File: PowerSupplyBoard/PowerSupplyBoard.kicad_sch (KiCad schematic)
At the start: 96 parts, among them J101 BATTERY, J102 I2C, J103 USB_C, J104 PWR, J105 DATA1, Q101 BSH205G2A, Q102 DMP6050SSD, Q103 2N7002H, SW101 SW_SPDT, U101 TPS63070, U102 MCP73834T, U103 NCV33163, U104 CYPD3177-24LQ, U105 CS5173

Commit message: psu rev5 layout
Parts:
- removed R134: 33k, Resistor_SMD:R_0805_2012Metric, symbol Device:R_US
- added D108: SMPS, LED_THT:LED_D3.0mm, symbol Device:LED
- added R135: 470, Resistor_SMD:R_0805_2012Metric, symbol Device:R_US
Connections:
- net +3.3V: now also D108.2 (A)
- net GND: now also R135.2
- new net: D108.1 (K), R135.1
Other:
- note removed: "R134 helps us discharge the decoupling caps after power down"
- moved on the sheet: C101, C102, C103, C104, C105, C107, C108, C110, C111, C112, C113, C114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

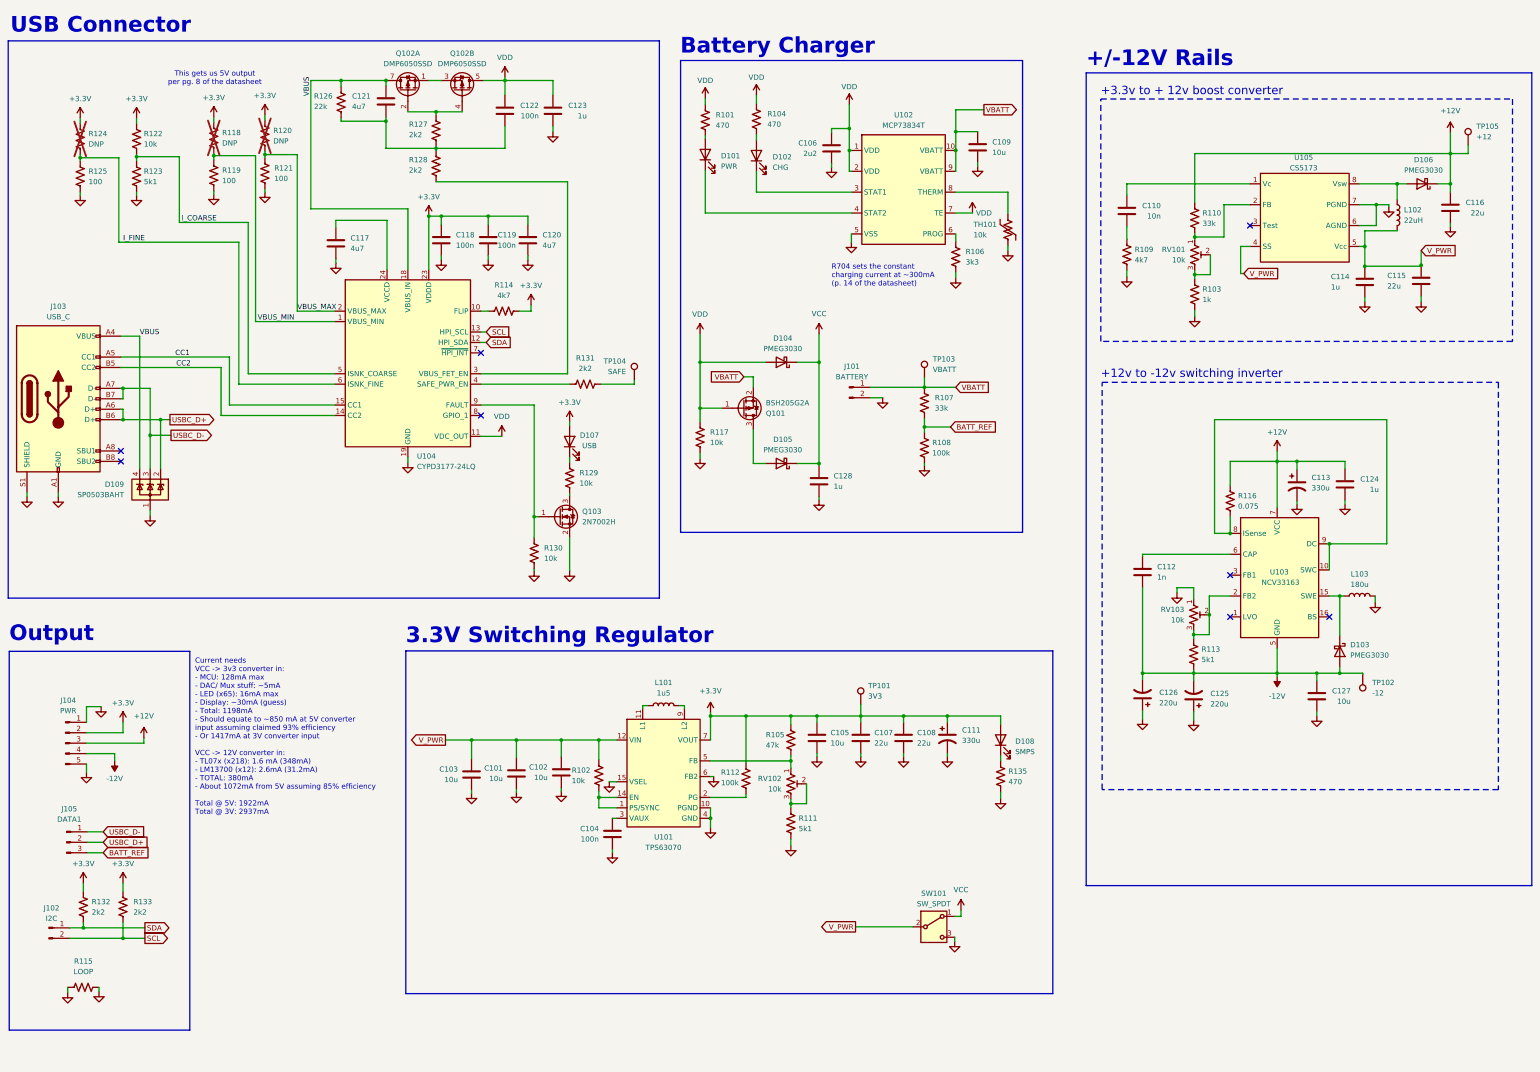
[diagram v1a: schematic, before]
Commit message: psu rev5 sent to fab
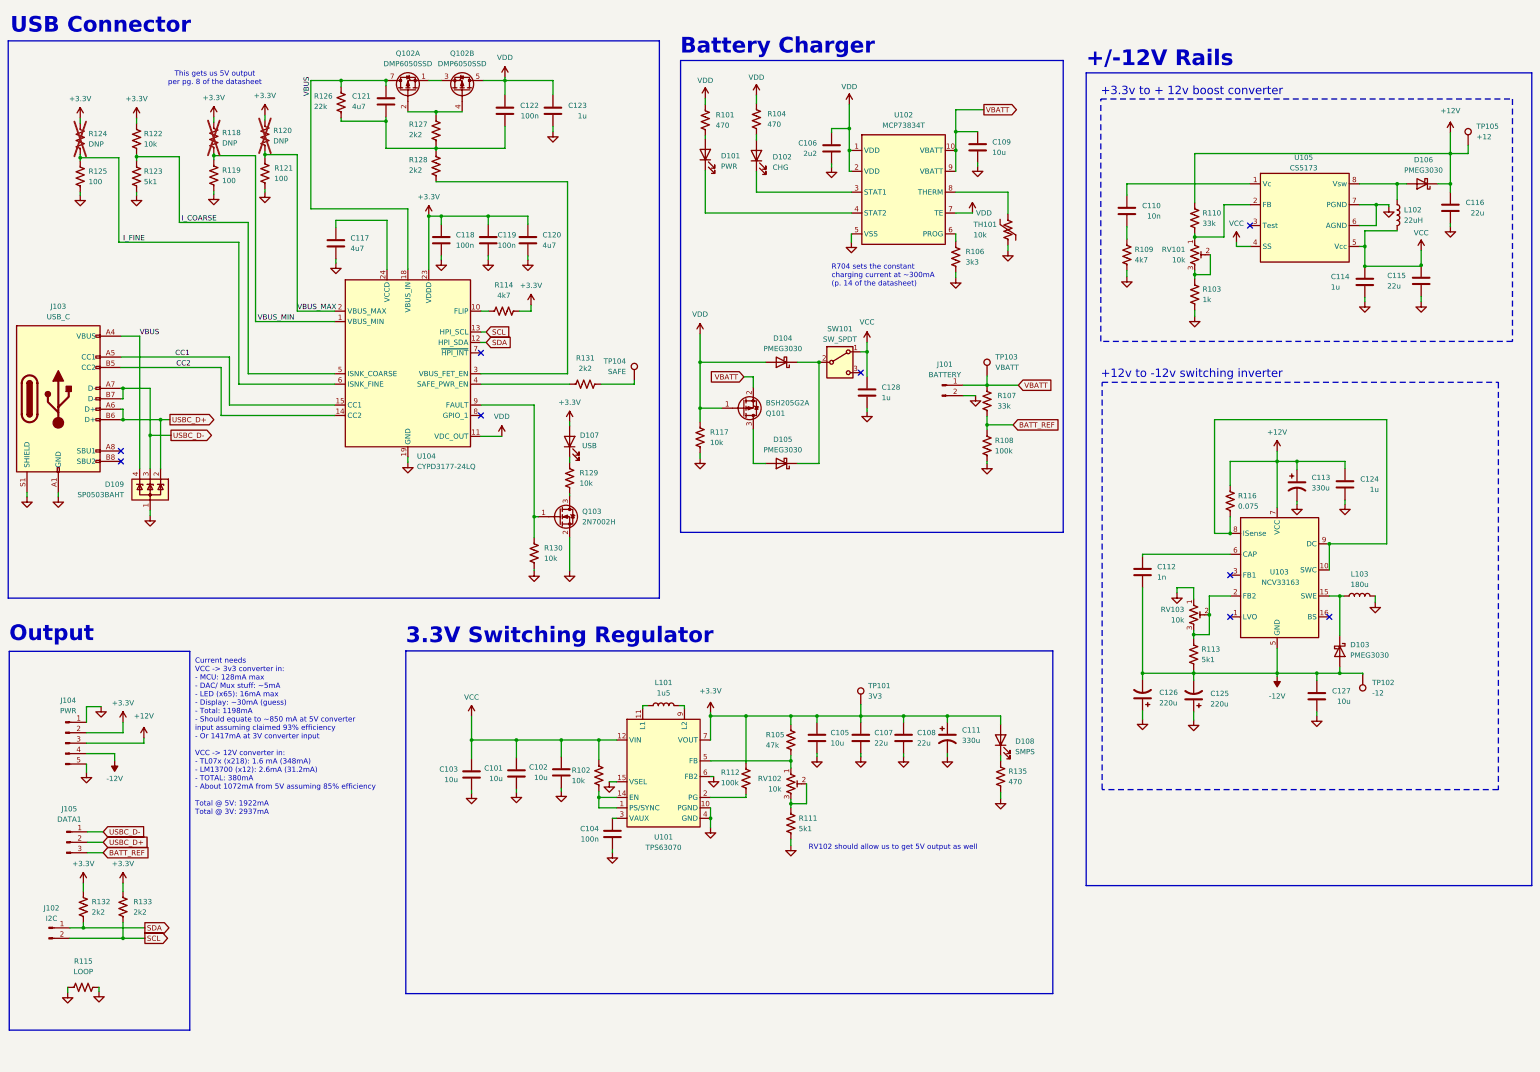
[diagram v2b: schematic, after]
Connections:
- net GND: no longer SW101.3 (C)
- net VCC: now also C101.1, C102.1, C103.1, C114.1, C115.1, L102.2, R102.1, U101.12 (VIN), U101.13 (VIN), U105.4 (SS), U105.5 (Vcc); no longer D104.1 (K), D105.1 (K)
- removed net VIN: C101.1, C102.1, C103.1, C114.1, C115.1, L102.2, R102.1, SW101.2 (B), U101.12 (VIN), U101.13 (VIN), U105.4 (SS), U105.5 (Vcc)
- new net: D104.1 (K), D105.1 (K), SW101.2 (B)
- no-connect marks 8 -> 9
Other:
- note added: "RV102 should allow us to get 5V output as well"
- moved on the sheet: C128, J101, R107, R108, SW101, TP103
